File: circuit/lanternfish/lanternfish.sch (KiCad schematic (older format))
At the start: 60 parts, among them J1 Input, J2 Prog, J3 Output, Q1 FQD17P06TM, Q2 PSMN5R6-60YLX, Q3 SI2302DDS-T1-GE3, SW1 SW_Push, SW2 SW_Push, SW3 PEC11R-4215F-S0024, SW4 SW_Push, SW5 SW_Push, SW6 SW_SPST, U1 MCP7940N-xMS, U2 L7805, U3 ATmega328PB-AU, Y1 ABS25-32.768KHZ-6-1-T

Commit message: Updated circuit [wip]
Removed 2 switches, connected MFP from RTC to MCU
Updated 25V netclass
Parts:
- removed C10, C11: 10uF, Capacitor_SMD:C_1206_3216Metric_Pad1.42x1.75mm_HandSolder, symbol Device:C
- removed R12, R13, R14: 10kR, Resistor_SMD:R_0805_2012Metric_Pad1.15x1.40mm_HandSolder, symbol Device:R
- removed SW4, SW5: SW_Push, Connector_PinHeader_2.54mm:PinHeader_1x02_P2.54mm_Vertical, symbol Switch:SW_Push
- added H1, H2, H3, H4: MountingHole, MountingHole:MountingHole_2.2mm_M2_Pad_Via, symbol Mechanical:MountingHole
- BT1: value Battery_Cell -> CR2032
- Q2: symbol Device:Q_NMOS_SSSGD -> lanternfish:Q_NMOS_SSSGD
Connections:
- net SW3 is gone; now on net RTC_MSP: U3.19 (PE2)
- net RTC_MSP: now reaches U1.7 (MFP)
- net RTC_MSP: now also R11.2
- net SW4: no longer names the net of U3.22 (PE3)
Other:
- moved on the sheet: BT1, C14, R15, R16, SW6

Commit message: Updated circuit
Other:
- note removed: "Note secondary GND for 25V ?\n"
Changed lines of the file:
@@
 PCINT24
-Wire Notes Line
-	10750 5700 8800 5700
 Wire Notes Line
 	8800 4450 10750 4450
@@
 Wire Notes Line
 	3700 4050 3700 5750
-Text Notes 9350 5800 0    50   ~ 0
-Note secondary GND for 25V ?\n
 $Comp
 L Mechanical:MountingHole H4
@@
 RTC_MSP
 NoConn ~ 5250 4300
+Wire Notes Line
+	10750 5700 8800 5700
 $EndSCHEMATC

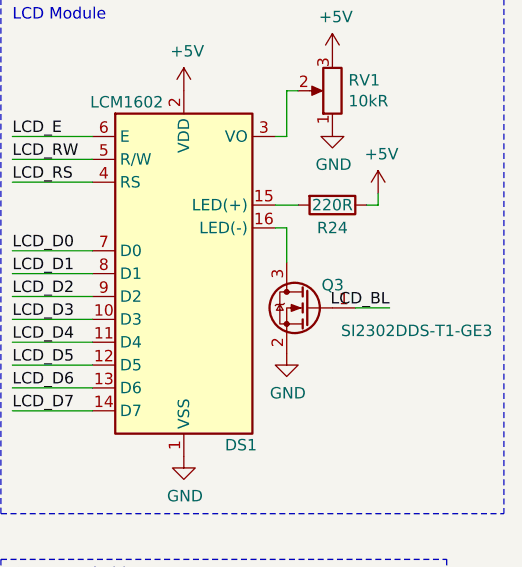
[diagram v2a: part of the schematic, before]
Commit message: Updated circuit
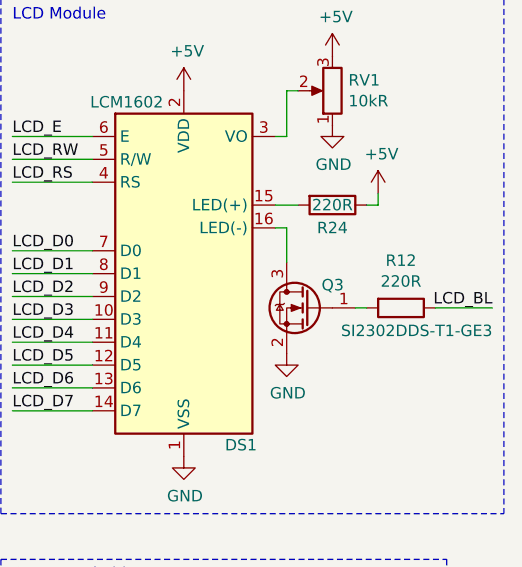
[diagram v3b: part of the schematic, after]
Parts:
- added R12: 220R, Resistor_SMD:R_1206_3216Metric_Pad1.42x1.75mm_HandSolder, symbol Device:R
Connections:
- net LCD_BL: now also R12.1; no longer Q3.1 (G)
- new net: Q3.1 (G), R12.2
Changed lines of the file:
@@
 	1    0    0    -1
 $EndComp
-Text Label 10500 3350 2    50   ~ 0
+Text Label 10950 3350 2    50   ~ 0
 LCD_BL
-Wire Wire Line
-	10500 3350 10350 3350
 Wire Notes Line
 	11000 2000 11000 4250
@@
 Wire Notes Line
 	10750 5700 8800 5700
+$Comp
+L Device:R R12
+U 1 1 5EF97E2C
+P 10550 3350
+F 0 "R12" V 10343 3350 50  0000 C CNN
+F 1 "220R" V 10434 3350 50  0000 C CNN
+F 2 "Resistor_SMD:R_1206_3216Metric_Pad1.42x1.75mm_HandSolder" V 10480 3350 50  0001 C CNN
+F 3 "~" H 10550 3350 50  0001 C CNN
+	1    10550 3350
+	0    1    1    0
+$EndComp
+Wire Wire Line
+	10400 3350 10350 3350
+Wire Wire Line
+	10950 3350 10700 3350
 $EndSCHEMATC
